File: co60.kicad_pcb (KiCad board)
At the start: 2 copper layers, 285 x 95.1 mm, 251 parts, among them J1 Conn_01x06, Q1 FMMT493TA, SW1 SW_Push, U1 ATMEGA32U4, Y1 16MHz

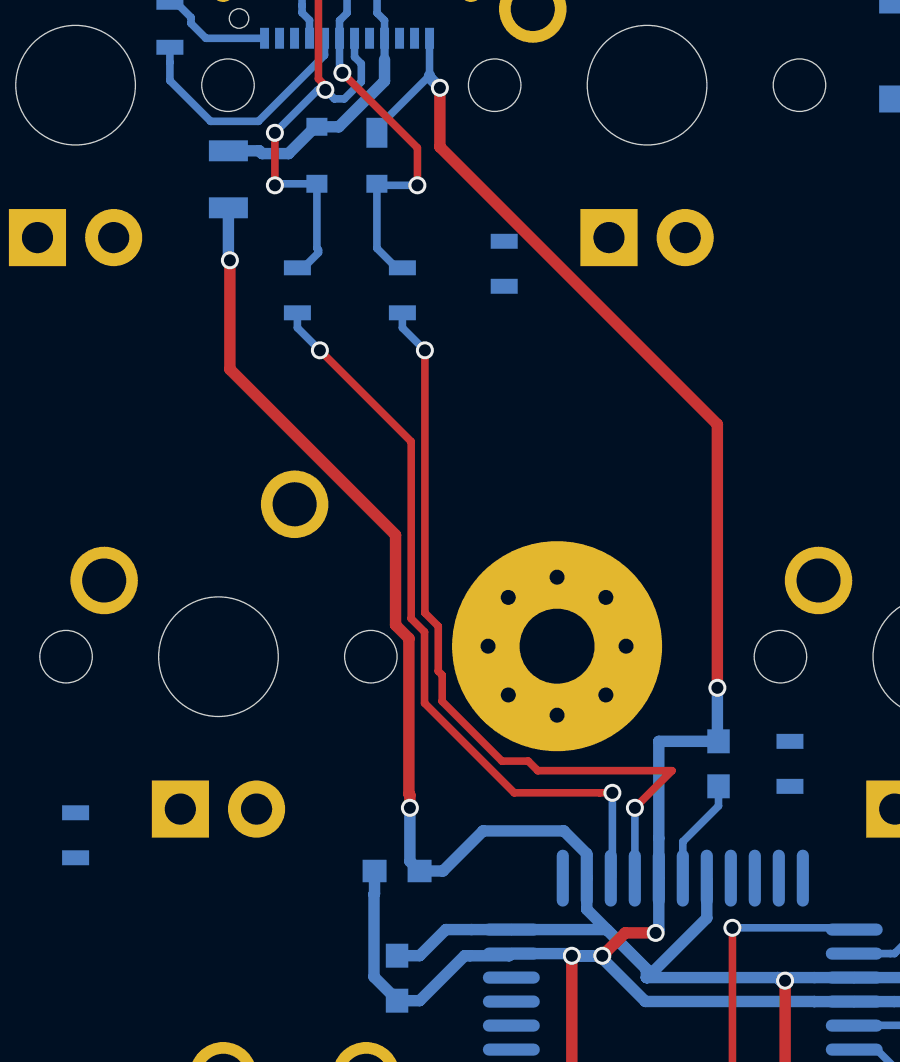
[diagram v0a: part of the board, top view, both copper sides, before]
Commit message: Update: Improve routing of USB data lines
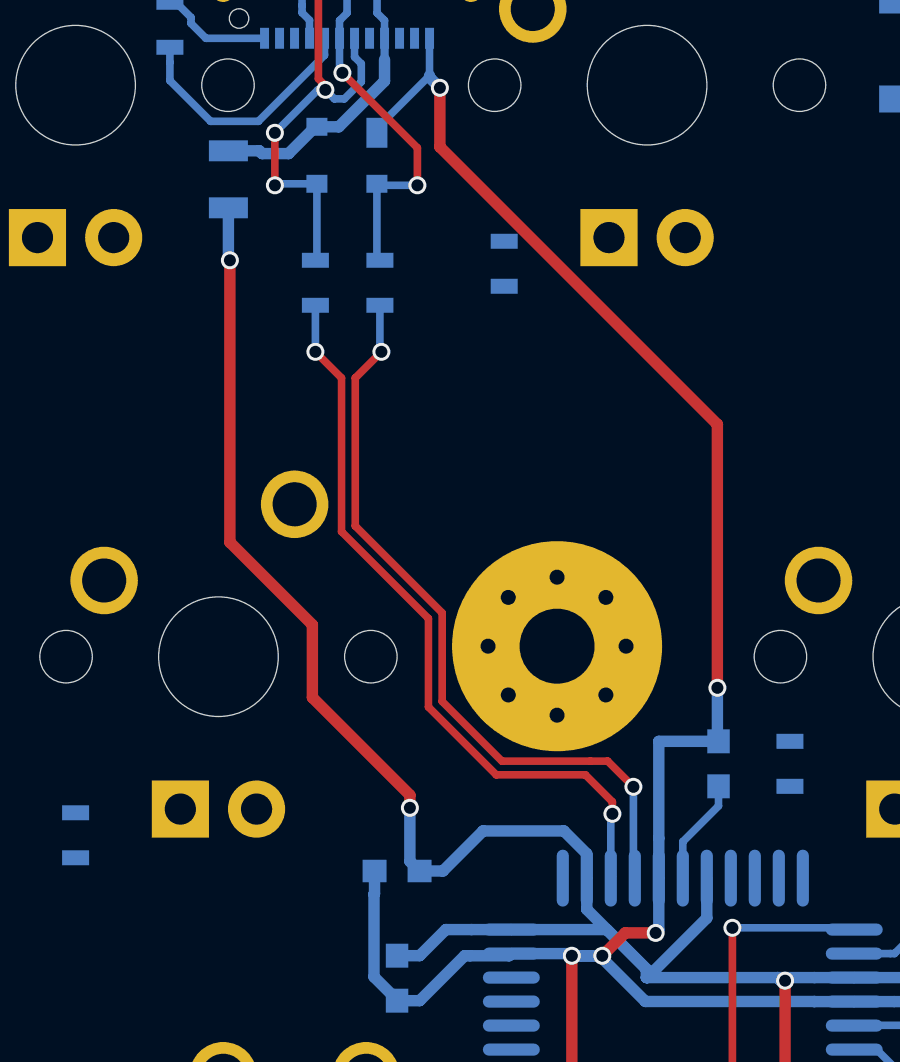
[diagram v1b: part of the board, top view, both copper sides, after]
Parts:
- moved RC4 0.79 mm to (98.2, 68.5)
- moved RC5 0.65 mm to (96.1, 68.5)
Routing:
- net D_P: track 27.0 -> 26.2 mm
- net Net-(DP1-Pad2): track 12.4 -> 11.7 mm
- net Net-(DP1-Pad3): track 18.3 -> 17.7 mm

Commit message: Add: Begin routing switch rows
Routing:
- net Net-(D63-Pad2): track 0.00 -> 31.8 mm
- net Net-(D62-Pad2): track 0.00 -> 24.3 mm
- net Net-(D44-Pad2): track 0.00 -> 21.7 mm
- net Net-(D65-Pad2): track 0.00 -> 18.3 mm
- net Net-(D56-Pad2): track 0.00 -> 17.6 mm
- net Net-(D61-Pad2): track 0.00 -> 16.7 mm
- net Net-(D30-Pad2): track 0.00 -> 16.2 mm
- net Net-(D67-Pad2): track 0.00 -> 13.9 mm
- net Net-(D15-Pad2): track 0.00 -> 13.9 mm
- net Net-(D16-Pad2): track 0.00 -> 11.4 mm
- net COL14: track 0.00 -> 10.6 mm
- net Net-(D57-Pad2): track 0.00 -> 9.69 mm
- net Net-(D60-Pad2): track 0.00 -> 9.52 mm
- net Net-(D59-Pad2): track 0.00 -> 9.52 mm
- net Net-(D58-Pad2): track 0.00 -> 9.52 mm
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
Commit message: Update: Work on routing switch matrix
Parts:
- moved R68 0.65 mm to (359.9, 143.5)
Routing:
- net ROW0: track 0.00 -> 317.6 mm
- net ROW3: track 0.00 -> 299.6 mm
- net ROW1: track 0.00 -> 299.6 mm
- net ROW4: track 0.00 -> 298.5 mm
- net ROW2: track 0.00 -> 246.0 mm
- net COL0: track 0.00 -> 112.6 mm, vias 0 -> 1
- net COL4: track 0.00 -> 109.2 mm
- net COL8: track 0.00 -> 107.0 mm
- net COL13: track 0.00 -> 106.9 mm
- net COL6: track 0.00 -> 104.7 mm
- net COL14: track 10.6 -> 105.3 mm
- net COL11: track 0.00 -> 94.1 mm
- net COL10: track 0.00 -> 94.0 mm
- net COL2: track 0.00 -> 92.3 mm
- net COL1: track 0.00 -> 91.3 mm, vias 0 -> 2
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
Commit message: Update: More routing and fix a schematic mistake
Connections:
- K_RCTL1 pad 3: Net-(K_RCTL1-Pad3) -> VCC
- K_RCTL1 pad 4: LEDGND -> Net-(K_RCTL1-Pad4)
- K_RCTL2 pad 3: Net-(K_RCTL1-Pad3) -> VCC
- K_RCTL2 pad 4: LEDGND -> Net-(K_RCTL1-Pad4)
- K_RCTL3 pad 3: Net-(K_RCTL1-Pad3) -> VCC
- K_RCTL3 pad 4: LEDGND -> Net-(K_RCTL1-Pad4)
- R68 pad 1: Net-(K_RCTL1-Pad3) -> Net-(K_RCTL1-Pad4)
- R68 pad 2: VCC -> LEDGND
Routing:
- net VCC: track 89.6 -> 430.8 mm, vias 4 -> 5
- net Net-(K_SPACE3_1-Pad4): track 0.00 -> 29.7 mm
- net Net-(K_SPACE2_1-Pad4): track 0.00 -> 29.5 mm
- net Net-(K_SPACE1_1-Pad4): track 0.00 -> 21.0 mm
- net Net-(K_RFN1-Pad4): track 0.00 -> 16.9 mm
- net Net-(K_RMOD1-Pad4): track 0.00 -> 13.6 mm
- net Net-(K_RCTL1-Pad4): track 0.00 -> 12.6 mm
- net Net-(K_LALT1-Pad4): track 0.00 -> 12.4 mm
- net Net-(K_LGUI1-Pad4): track 0.00 -> 12.3 mm
- net Net-(K_C1-Pad3): track 0.00 -> 12.1 mm
- net Net-(K_LCTL1-Pad4): track 0.00 -> 11.8 mm
- net LEDGND: track 8.31 -> 0.00 mm
- net Net-(K_RALT1-Pad4): track 0.00 -> 6.70 mm
- net Net-(K_Y1-Pad4): track 0.00 -> 4.87 mm
- net Net-(K_]1-Pad4): track 0.00 -> 4.87 mm
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
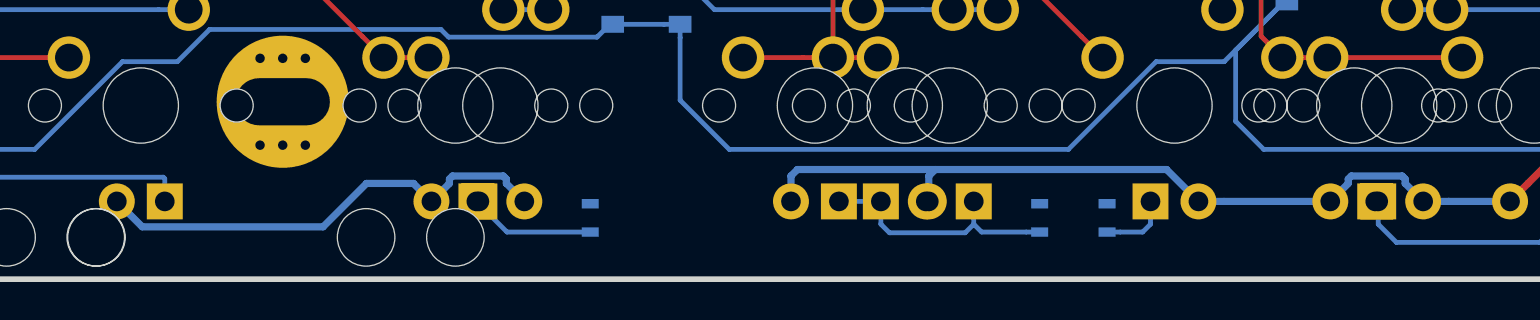
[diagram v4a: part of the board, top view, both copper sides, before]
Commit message: Update: Undo some questionable routing
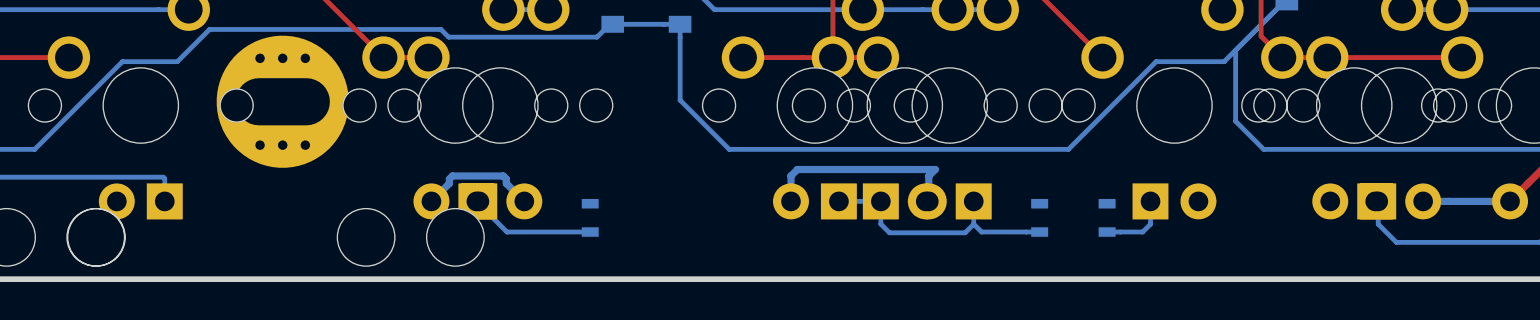
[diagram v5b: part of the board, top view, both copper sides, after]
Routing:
- net VCC: track 430.8 -> 384.3 mm
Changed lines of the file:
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@@
   (general
     (links 572)
-    (no_connects 164)
+    (no_connects 167)
     (area 0 0 0 0)
     (thickness 1.6)
     (drawings 0)
-    (tracks 1540)
+    (tracks 1524)
     (zones 0)
     (modules 251)
@@
   (segment (start 218.839212 143.1925) (end 215.5825 143.1925) (width 0.381) (layer B.Cu) (net 5))
   (segment (start 244.1575 143.1925) (end 246.38 143.1925) (width 0.381) (layer B.Cu) (net 5))
-  (segment (start 260.6675 143.1925) (end 262.013701 144.538701) (width 0.381) (layer B.Cu) (net 5))
-  (segment (start 262.013701 144.538701) (end 271.596101 144.538701) (width 0.381) (layer B.Cu) (net 5))
-  (segment (start 271.596101 144.538701) (end 273.894801 142.240001) (width 0.381) (layer B.Cu) (net 5))
-  (segment (start 273.894801 142.240001) (end 276.383751 142.240001) (width 0.381) (layer B.Cu) (net 5))
-  (segment (start 276.383751 142.240001) (end 277.33625 143.1925) (width 0.381) (layer B.Cu) (net 5))
   (segment (start 277.33625 143.1925) (end 278.288749 142.240001) (width 0.381) (layer B.Cu) (net 5))
   (segment (start 278.288749 142.240001) (end 278.288749 142.007589) (width 0.381) (layer B.Cu) (net 5))
@@
   (segment (start 296.38625 143.1925) (end 296.38625 141.845462) (width 0.381) (layer B.Cu) (net 5))
   (segment (start 296.38625 141.845462) (end 296.728312 141.5034) (width 0.381) (layer B.Cu) (net 5))
-  (segment (start 304.030812 141.5034) (end 316.28715 141.5034) (width 0.381) (layer B.Cu) (net 5))
-  (segment (start 316.28715 141.5034) (end 317.97625 143.1925) (width 0.381) (layer B.Cu) (net 5))
   (segment (start 303.68875 143.1925) (end 303.68875 141.845462) (width 0.381) (layer B.Cu) (net 5))
   (segment (start 303.68875 141.845462) (end 304.030812 141.5034) (width 0.381) (layer B.Cu) (net 5))
-  (segment (start 317.97625 143.1925) (end 319.323288 143.1925) (width 0.381) (layer B.Cu) (net 5))
-  (segment (start 319.323288 143.1925) (end 324.96125 143.1925) (width 0.381) (layer B.Cu) (net 5))
   (segment (start 339.4075 124.1425) (end 339.4075 125.489538) (width 0.381) (layer F.Cu) (net 5))
   (segment (start 339.4075 125.489538) (end 336.777549 128.119489) (width 0.381) (layer F.Cu) (net 5))
@@
   (segment (start 338.143851 139.534899) (end 335.438749 142.240001) (width 0.381) (layer F.Cu) (net 5))
   (segment (start 335.438749 142.240001) (end 334.48625 143.1925) (width 0.381) (layer F.Cu) (net 5))
-  (segment (start 324.96125 143.1925) (end 325.913749 142.240001) (width 0.381) (layer B.Cu) (net 5))
-  (segment (start 328.930001 142.007589) (end 328.930001 142.240001) (width 0.381) (layer B.Cu) (net 5))
-  (segment (start 325.913749 142.240001) (end 325.913749 142.007589) (width 0.381) (layer B.Cu) (net 5))
-  (segment (start 325.913749 142.007589) (end 326.075039 141.846299) (width 0.381) (layer B.Cu) (net 5))
-  (segment (start 326.075039 141.846299) (end 328.768711 141.846299) (width 0.381) (layer B.Cu) (net 5))
-  (segment (start 328.768711 141.846299) (end 328.930001 142.007589) (width 0.381) (layer B.Cu) (net 5))
-  (segment (start 328.930001 142.240001) (end 329.8825 143.1925) (width 0.381) (layer B.Cu) (net 5))
   (segment (start 329.8825 143.1925) (end 331.229538 143.1925) (width 0.381) (layer B.Cu) (net 5))
   (segment (start 331.229538 143.1925) (end 334.48625 143.1925) (width 0.381) (layer B.Cu) (net 5))

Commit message: Update: Work on routing LED connections
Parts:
- moved SW1 30.8 mm to (107.1, 110.7), turned to 270 degrees
- moved R68 14.5 mm to (345.4, 144.3)
- moved Q1 8.59 mm to (100.1, 110.2)
- moved R67 8.46 mm to (332.1, 144.9), turned to 270 degrees
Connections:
- K_C1 pad 3: Net-(K_C1-Pad3) -> VCC
- K_D1 pad 3: Net-(K_C1-Pad3) -> VCC
- K_E1 pad 3: Net-(K_C1-Pad3) -> VCC
- K_SPACE1_1 pad 3: Net-(K_C1-Pad3) -> VCC
- K_SPACE1_2 pad 3: Net-(K_C1-Pad3) -> VCC
- K_SPACE1_3 pad 3: Net-(K_C1-Pad3) -> VCC
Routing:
- net VCC: track 384.3 -> 1543.8 mm, vias 5 -> 9
- net Net-(J1-Pad2): track 5.01 -> 32.3 mm, vias 0 -> 2
- net GND: track 153.9 -> 174.6 mm, vias 7 -> 9
- net Net-(K_C1-Pad3): track 12.1 -> 0.00 mm
- net Net-(Q1-Pad2): track 2.33 -> 10.1 mm
- net Net-(K_W1-Pad4): track 0.00 -> 4.87 mm
- net Net-(K_TAB1-Pad4): track 0.00 -> 4.87 mm
- net Net-(K_E1-Pad4): track 0.00 -> 4.87 mm
- net Net-(K_RFN1-Pad4): track 16.9 -> 12.3 mm
- net Net-(K_Q1-Pad4): track 0.00 -> 4.10 mm
- net Net-(K_RCTL1-Pad4): track 12.6 -> 15.7 mm
- net COL12: track 90.8 -> 87.8 mm
- net COL0: track 112.6 -> 110.8 mm
- net COL4: track 109.2 -> 107.7 mm
- net COL1: track 91.3 -> 90.4 mm

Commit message: Update: More routing
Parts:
- moved R61 30.1 mm to (196.6, 144.1), turned to 90 degrees
- moved R68 1.63 mm to (346.7, 145.3)
- moved C7 0.57 mm to (114.2, 102.3)
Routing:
- net LEDGND: track 0.00 -> 1434.0 mm, vias 0 -> 12
- net COL14: track 105.3 -> 356.9 mm
- net COL13: track 106.9 -> 326.4 mm, vias 0 -> 1
- net COL12: track 87.8 -> 292.7 mm, vias 0 -> 1
- net COL11: track 94.1 -> 291.8 mm, vias 0 -> 1
- net COL10: track 94.0 -> 262.6 mm, vias 0 -> 1
- net COL9: track 67.9 -> 218.2 mm, vias 0 -> 1
- net COL8: track 107.0 -> 227.7 mm, vias 0 -> 1
- net COL7: track 67.9 -> 170.6 mm, vias 0 -> 3
- net COL6: track 104.7 -> 196.7 mm, vias 0 -> 3
- net COL5: track 67.0 -> 142.9 mm, vias 0 -> 1
- net COL4: track 107.7 -> 168.9 mm, vias 0 -> 5
- net ROW0: track 317.6 -> 376.3 mm, vias 0 -> 2
- net COL3: track 67.3 -> 106.9 mm, vias 0 -> 3
- net ROW1: track 299.6 -> 330.8 mm, vias 0 -> 2
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
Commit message: Update: Still more routing
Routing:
- net ROW2: track 246.0 -> 263.8 mm
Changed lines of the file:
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@@
     (thickness 1.6)
     (drawings 0)
-    (tracks 2473)
+    (tracks 2480)
     (zones 0)
     (modules 251)
@@
   (segment (start 352.58375 75.8825) (end 353.91625 74.55) (width 0.254) (layer B.Cu) (net 36))
   (segment (start 353.91625 74.55) (end 355.996875 74.55) (width 0.254) (layer B.Cu) (net 36))
+  (segment (start 114.061875 96.459675) (end 114.808635 96.459675) (width 0.254) (layer B.Cu) (net 37))
+  (segment (start 114.808635 96.459675) (end 115.251011 96.017299) (width 0.254) (layer B.Cu) (net 37))
+  (segment (start 120.369037 97.688399) (end 126.140649 97.688399) (width 0.254) (layer B.Cu) (net 37))
+  (segment (start 115.251011 96.017299) (end 118.697937 96.017299) (width 0.254) (layer B.Cu) (net 37))
+  (segment (start 118.697937 96.017299) (end 120.369037 97.688399) (width 0.254) (layer B.Cu) (net 37))
+  (segment (start 126.140649 97.688399) (end 128.924125 100.471875) (width 0.254) (layer B.Cu) (net 37))
+  (segment (start 128.924125 100.471875) (end 129.778125 100.471875) (width 0.254) (layer B.Cu) (net 37))
   (segment (start 302.699575 100.471875) (end 302.082125 100.471875) (width 0.254) (layer B.Cu) (net 37))
   (segment (start 317.559399 102.336601) (end 304.564301 102.336601) (width 0.254) (layer B.Cu) (net 37))
